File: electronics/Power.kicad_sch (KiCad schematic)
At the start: 27 parts, among them J2 Conn_01x02_Socket, Q2 IRLML6401, U10 AOZ1280CI, U4 ANT13SECQE, U5 LM1117DT-ADJ, U7 LM1117DT-ADJ

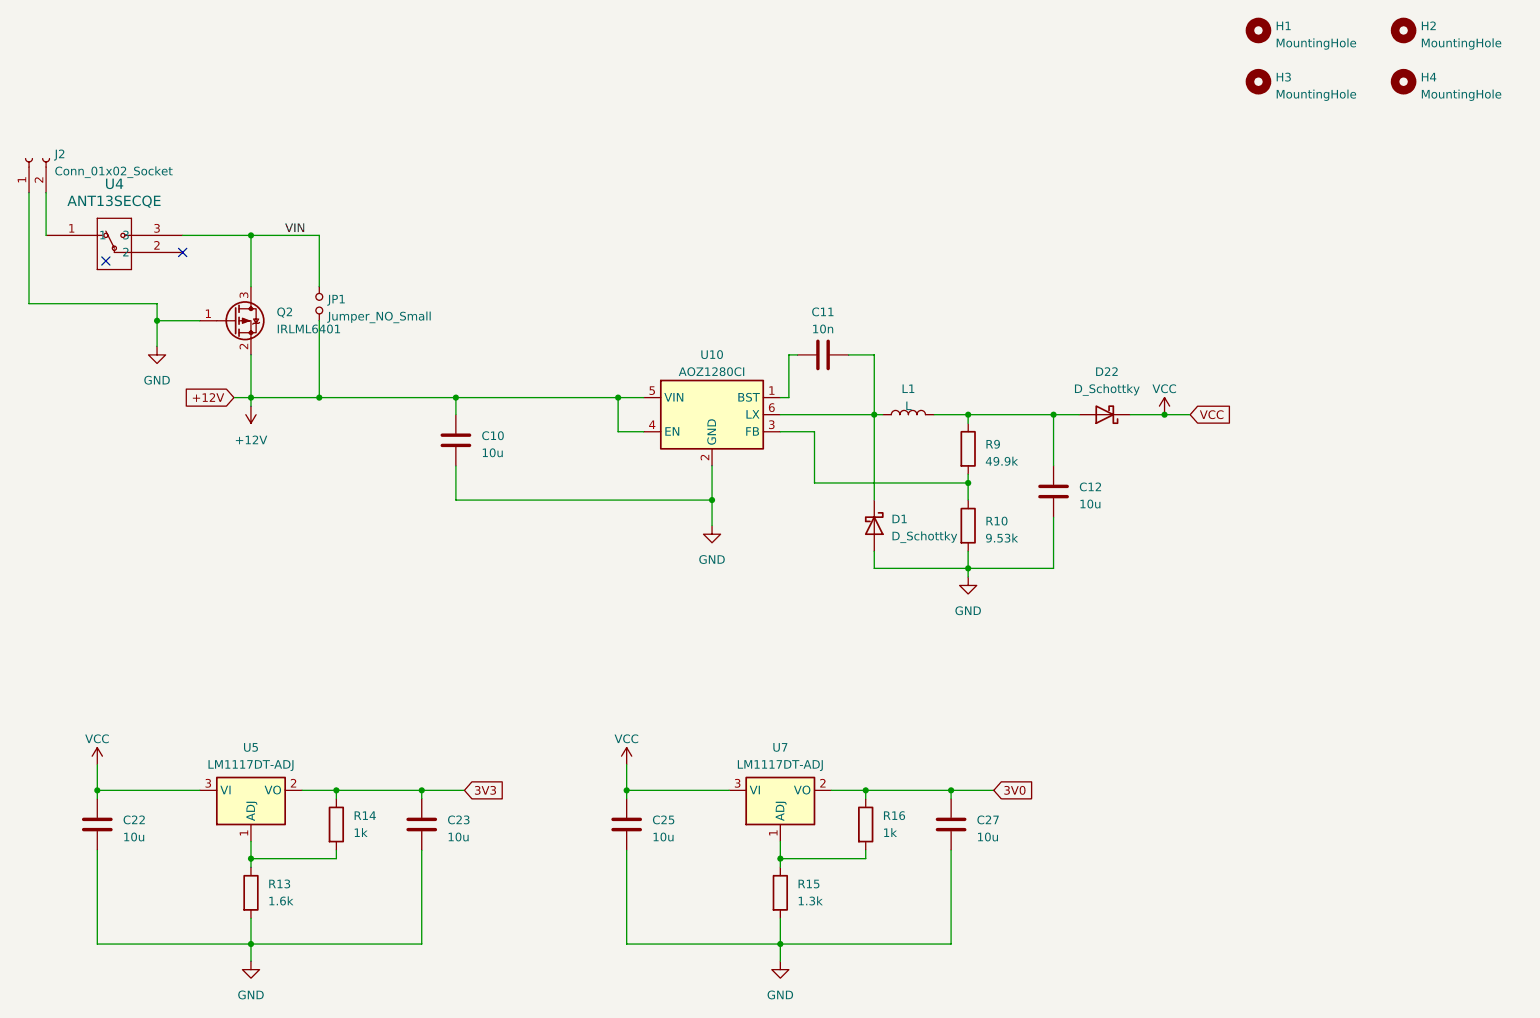
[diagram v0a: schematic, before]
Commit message: Many changes to the design. Fully routed.
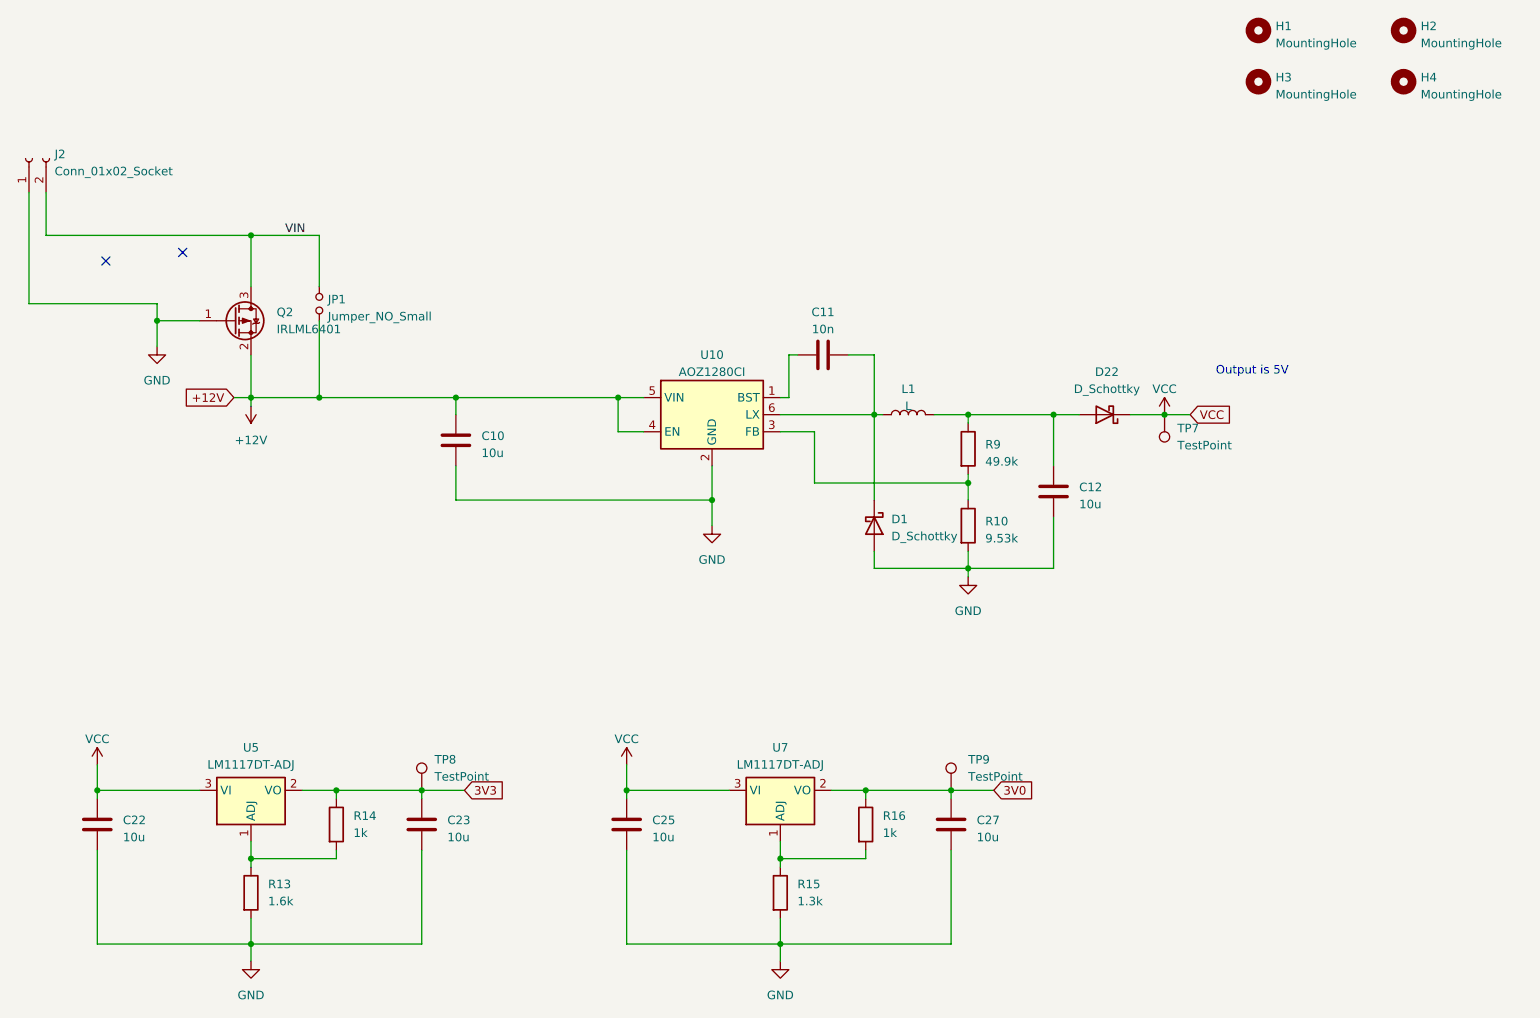
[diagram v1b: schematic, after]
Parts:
- removed U4: ANT13SECQE, footprints:ANT13SEC_CRS, symbol General:ANT13SECQE
- added TP7, TP8, TP9: TestPoint, TestPoint:TestPoint_Pad_D1.0mm, symbol Connector:TestPoint
- J2: footprint Connector_USB:USB_Micro-B_Amphenol_10118193-0001LF_Horizontal -> Connector_Phoenix_MSTB:PhoenixContact_MSTBVA_2,5_2-G_1x02_P5.00mm_Vertical
- R10, R13, R14, R15, R16, R9: footprint Resistor_SMD:R_0603_1608Metric_Pad0.98x0.95mm_HandSolder -> Resistor_SMD:R_0402_1005Metric
- U5, U7: footprint Package_TO_SOT_SMD:TO-252-3_TabPin2 -> Package_TO_SOT_SMD:SOT-223-3_TabPin2
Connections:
- net 3V0: now also TP9.1
- net 3V3: now also TP8.1
- net VCC: now also TP7.1
- net VIN: now also J2.2 (Pin_2)
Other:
- note added: "Output is 5V"

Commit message: Almost sent this to fab. It is getting expensive.
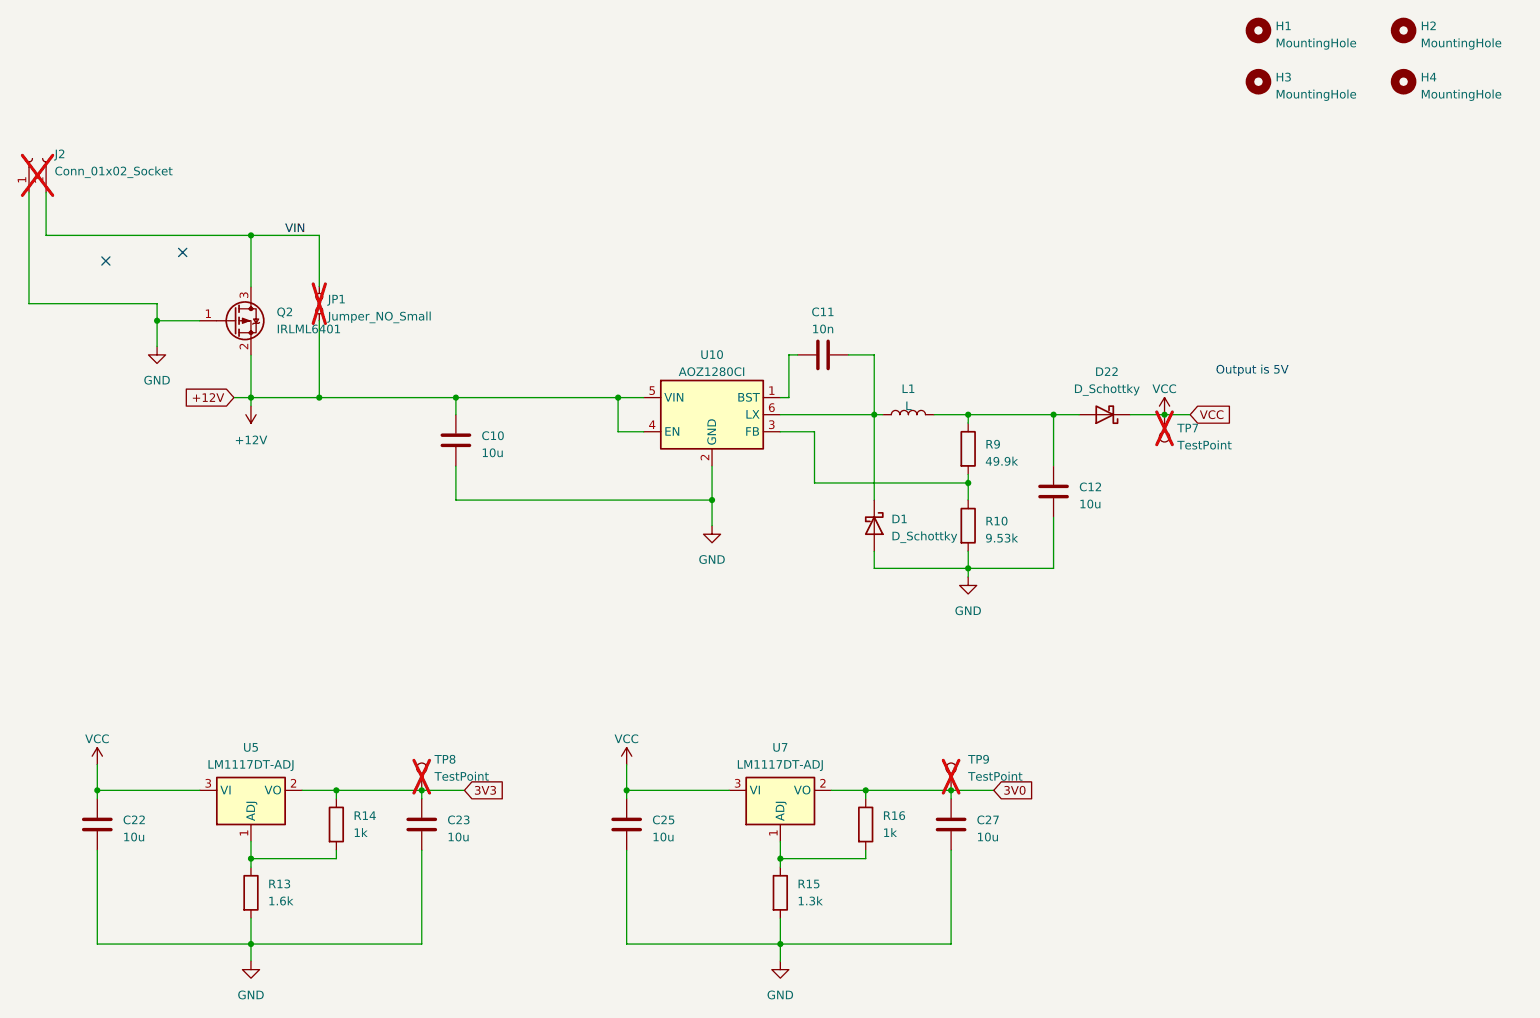
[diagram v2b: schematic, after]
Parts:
- J2, JP1, TP7, TP8, TP9: now not fitted
- R10: JLCPCB (none) -> C321660
- R13: JLCPCB (none) -> C412995
- R14, R16: JLCPCB (none) -> C11702
- R15: JLCPCB (none) -> C172154
- R9: JLCPCB (none) -> C103072

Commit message: Ordered this version.
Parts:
- D1, D22: JLCPCB C130887 -> C7420325
- H1, H2, H3, H4: now not fitted
- L1: JLCPCB C576538 -> C1330201
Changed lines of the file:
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@@
 		(in_bom yes)
 		(on_board yes)
-		(dnp no)
+		(dnp yes)
 		(fields_autoplaced yes)
 		(property "Reference" "H3"
@@
 		(in_bom yes)
 		(on_board yes)
-		(dnp no)
+		(dnp yes)
 		(fields_autoplaced yes)
 		(property "Reference" "H4"
@@
 			)
 		)
-		(property "JLCPCB" "C130887"
+		(property "JLCPCB" "C7420325"
 			(at 207.01 81.28 0)
 			(effects
@@
 			)
 		)
-		(property "JLCPCB" "C130887"
+		(property "JLCPCB" "C7420325"
 			(at 172.72 97.79 0)
 			(effects
@@
 		(in_bom yes)
 		(on_board yes)
-		(dnp no)
+		(dnp yes)
 		(fields_autoplaced yes)
 		(property "Reference" "H2"
@@
 		(in_bom yes)
 		(on_board yes)
-		(dnp no)
+		(dnp yes)
 		(fields_autoplaced yes)
 		(property "Reference" "H1"
@@
 			)
 		)
-		(property "JLCPCB" "C576538"
+		(property "JLCPCB" "C1330201"
 			(at 177.8 81.28 0)
 			(effects

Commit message: Tweaked parts to use Basic parts which are cheaper.
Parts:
- D1, D22: JLCPCB C7420325 -> C8598
- R10: footprint Resistor_SMD:R_0402_1005Metric -> Resistor_SMD:R_0603_1608Metric; JLCPCB C321660 -> (none)
- R13: footprint Resistor_SMD:R_0402_1005Metric -> Resistor_SMD:R_0603_1608Metric; JLCPCB C412995 -> C102825
- R14, R16: JLCPCB C11702 -> (none)
- R15: footprint Resistor_SMD:R_0402_1005Metric -> Resistor_SMD:R_0603_1608Metric; JLCPCB C172154 -> (none)
- R9: footprint Resistor_SMD:R_0402_1005Metric -> Resistor_SMD:R_0603_1608Metric; JLCPCB C103072 -> (none)
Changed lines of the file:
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@@
 			)
 		)
-		(property "Footprint" "Resistor_SMD:R_0402_1005Metric"
+		(property "Footprint" "Resistor_SMD:R_0603_1608Metric"
 			(at 184.912 86.36 90)
 			(effects
@@
 			)
 		)
-		(property "JLCPCB" "C103072"
+		(property "JLCPCB" ""
 			(at 186.69 86.36 0)
 			(effects
@@
 			)
 		)
-		(property "Footprint" "Resistor_SMD:R_0402_1005Metric"
+		(property "Footprint" "Resistor_SMD:R_0603_1608Metric"
 			(at 156.972 152.4 90)
 			(effects
@@
 			)
 		)
-		(property "JLCPCB" "C172154"
+		(property "JLCPCB" ""
 			(at 158.75 152.4 0)
 			(effects
@@
 			)
 		)
-		(property "JLCPCB" "C7420325"
+		(property "JLCPCB" "C8598"
 			(at 207.01 81.28 0)
 			(effects
@@
 			)
 		)
-		(property "JLCPCB" "C11702"
+		(property "JLCPCB" ""
 			(at 171.45 142.24 0)
 			(effects
@@
 			)
 		)
-		(property "JLCPCB" "C7420325"
+		(property "JLCPCB" "C8598"
 			(at 172.72 97.79 0)
 			(effects
@@
 			)
 		)
-		(property "Footprint" "Resistor_SMD:R_0402_1005Metric"
+		(property "Footprint" "Resistor_SMD:R_0603_1608Metric"
 			(at 78.232 152.4 90)
 			(effects
@@
 			)
 		)
-		(property "JLCPCB" "C412995"
+		(property "JLCPCB" "C102825"
 			(at 80.01 152.4 0)
 			(effects
@@
 		(dnp no)
 		(fields_autoplaced yes)
-		(property "Reference" "#PWR05"
+		(property "Reference" "#PWR046"
 			(at 80.01 76.2 0)
 			(effects
@@
 		(dnp no)
 		(fields_autoplaced yes)
-		(property "Reference" "#PWR06"
+		(property "Reference" "#PWR045"
 			(at 66.04 77.47 0)
 			(effects
@@
 			)
 		)
-		(property "JLCPCB" "C11702"
+		(property "JLCPCB" ""
 			(at 92.71 142.24 0)
 			(effects
@@
 			)
 		)
-		(property "Footprint" "Resistor_SMD:R_0402_1005Metric"
+		(property "Footprint" "Resistor_SMD:R_0603_1608Metric"
 			(at 184.912 97.79 90)
 			(effects
@@
 			)
 		)
-		(property "JLCPCB" "C321660"
+		(property "JLCPCB" ""
 			(at 186.69 97.79 0)
 			(effects

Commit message: Ordered this version.
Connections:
- no-connect marks 2 -> 0
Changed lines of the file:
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@@
 		(color 0 0 0 0)
-	)
-	(no_connect
-		(at 69.85 57.15)
-	)
-	(no_connect
-		(at 58.42 58.42)
 	)
 	(wire

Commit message: Updated design for REV B.
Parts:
- removed H1, H2, H3, H4: MountingHole, MountingHole:MountingHole_4.3mm_M4, symbol Mechanical:MountingHole
- C11: JLCPCB (none) -> C57112
- J2: footprint Connector_Phoenix_MSTB:PhoenixContact_MSTBVA_2,5_2-G_1x02_P5.00mm_Vertical -> Connector_JST:JST_PH_S2B-PH-K_1x02_P2.00mm_Horizontal; JLCPCB (none) -> C173752; now fitted

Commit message: This version is working well. Need to figure out USB DFU programming.
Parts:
- C10, C12, C22, C23, C25, C27: JLCPCB C96446 -> C15850
- C11: footprint Capacitor_SMD:C_0603_1608Metric -> Capacitor_SMD:C_0402_1005Metric; JLCPCB C57112 -> C15195
- J2: Digikey (none) -> 455-1719-ND
- L1: footprint Inductor_SMD:L_Taiyo-Yuden_MD-3030 -> Inductor_SMD:L_1210_3225Metric
- R10: footprint Resistor_SMD:R_0603_1608Metric -> Resistor_SMD:R_0402_1005Metric; JLCPCB (none) -> C103191
- R13: footprint Resistor_SMD:R_0603_1608Metric -> Resistor_SMD:R_0402_1005Metric
- R14, R16: JLCPCB (none) -> C11702
- R15: footprint Resistor_SMD:R_0603_1608Metric -> Resistor_SMD:R_0402_1005Metric; JLCPCB (none) -> C4906
- R9: footprint Resistor_SMD:R_0603_1608Metric -> Resistor_SMD:R_0402_1005Metric; JLCPCB (none) -> C100457
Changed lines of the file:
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@@
 			)
 		)
-		(property "JLCPCB" "C96446"
+		(property "JLCPCB" "C15850"
 			(at 105.41 142.24 0)
 			(effects
@@
 			)
 		)
-		(property "JLCPCB" "C96446"
+		(property "JLCPCB" "C15850"
 			(at 57.15 142.24 0)
 			(effects
@@
 			)
 		)
-		(property "Footprint" "Resistor_SMD:R_0603_1608Metric"
+		(property "Footprint" "Resistor_SMD:R_0402_1005Metric"
 			(at 184.912 86.36 90)
 			(effects
@@
 			)
 		)
-		(property "JLCPCB" ""
+		(property "JLCPCB" "C100457"
 			(at 186.69 86.36 0)
 			(effects
@@
 			)
 		)
-		(property "Footprint" "Resistor_SMD:R_0603_1608Metric"
+		(property "Footprint" "Resistor_SMD:R_0402_1005Metric"
 			(at 156.972 152.4 90)
 			(effects
@@
 			)
 		)
-		(property "JLCPCB" ""
+		(property "JLCPCB" "C4906"
 			(at 158.75 152.4 0)
 			(effects
@@
 			)
 		)
-		(property "JLCPCB" "C96446"
+		(property "JLCPCB" "C15850"
 			(at 110.49 85.09 0)
 			(effects
@@
 			)
 		)
-		(property "JLCPCB" "C96446"
+		(property "JLCPCB" "C15850"
 			(at 199.39 92.71 0)
 			(effects
@@
 			)
 		)
-		(property "Footprint" "Capacitor_SMD:C_0603_1608Metric"
+		(property "Footprint" "Capacitor_SMD:C_0402_1005Metric"
 			(at 168.91 71.4248 0)
 			(effects
@@
 			)
 		)
-		(property "JLCPCB" "C57112"
+		(property "JLCPCB" "C15195"
 			(at 165.1 72.39 0)
 			(effects
@@
 			)
 		)
-		(property "JLCPCB" ""
+		(property "JLCPCB" "C11702"
 			(at 171.45 142.24 0)
 			(effects
@@
 			)
 		)
-		(property "Footprint" "Resistor_SMD:R_0603_1608Metric"
+		(property "Footprint" "Resistor_SMD:R_0402_1005Metric"
 			(at 78.232 152.4 90)
 			(effects
@@
 			)
 		)
-		(property "JLCPCB" "C96446"
+		(property "JLCPCB" "C15850"
 			(at 184.15 142.24 0)
 			(effects
@@
 			)
 		)
+		(property "Digikey" "455-1719-ND"
+			(at 46.99 43.18 0)
+			(effects
+				(font
+					(size 1.27 1.27)
+				)
+				(hide yes)
+			)
+		)
 		(pin "1"
 		)
@@
 			)
 		)
-		(property "JLCPCB" ""
+		(property "JLCPCB" "C11702"
 			(at 92.71 142.24 0)
 			(effects
@@
 			)
 		)
-		(property "Footprint" "Inductor_SMD:L_Taiyo-Yuden_MD-3030"
+		(property "Footprint" "Inductor_SMD:L_1210_3225Metric"
 			(at 177.8 81.28 0)
 			(effects
@@
 			)
 		)
-		(property "Footprint" "Resistor_SMD:R_0603_1608Metric"
+		(property "Footprint" "Resistor_SMD:R_0402_1005Metric"
 			(at 184.912 97.79 90)
 			(effects
@@
 			)
 		)
-		(property "JLCPCB" ""
+		(property "JLCPCB" "C103191"
 			(at 186.69 97.79 0)
 			(effects
@@
 			)
 		)
-		(property "JLCPCB" "C96446"
+		(property "JLCPCB" "C15850"
 			(at 135.89 142.24 0)
 			(effects
